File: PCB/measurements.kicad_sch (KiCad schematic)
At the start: 32 parts

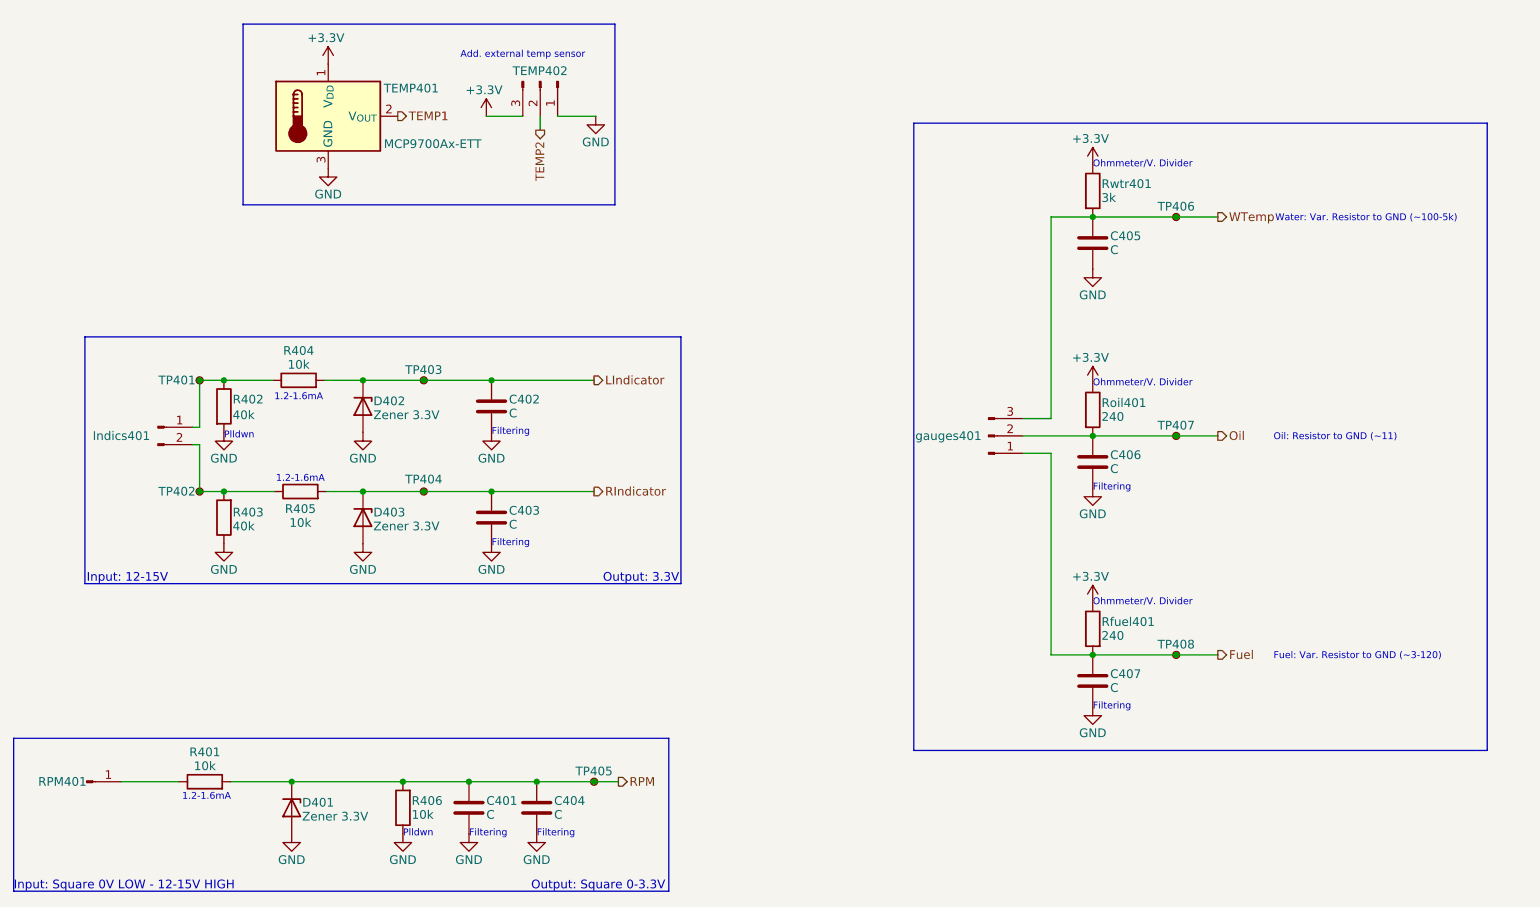
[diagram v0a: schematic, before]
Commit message: Applied recommendations from my coworker; Fixed badly placed filter caps; Added flyback diode to fan circuit; Applied larger grid and some spacing to the schematics; And some other small adjustments
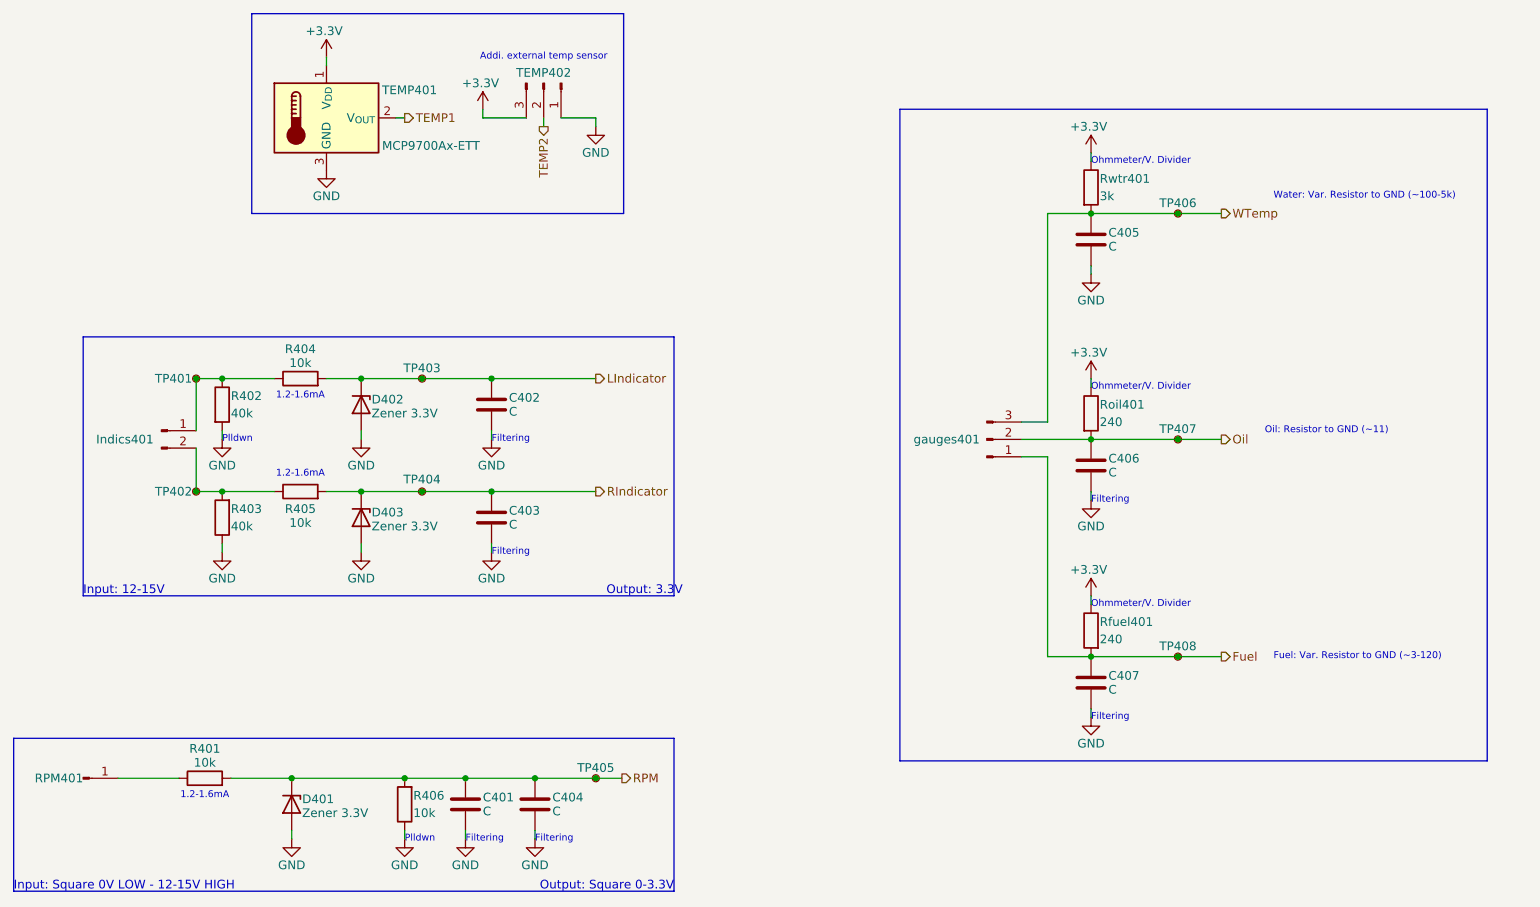
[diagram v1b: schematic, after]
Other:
- note added: "Addi. external temp sensor"
- note removed: "Add. external temp sensor"
- title: (none) -> Measurements
- moved on the sheet: C401, C404, C405, C406, D401, Indics401, R401, R406, RPM401, Roil401, Rwtr401, TEMP402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

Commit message: Changed some resistor and capacitor values;Added additional input electrolytic cap;Selected LCSC parts;Added diode footprint;Removed 3.3V power supply and decreased the output of the 5V supply to 3.3V;Added flyback diode on the fan circuit;Added LDO between the USB-C VBUS and the 5V rail
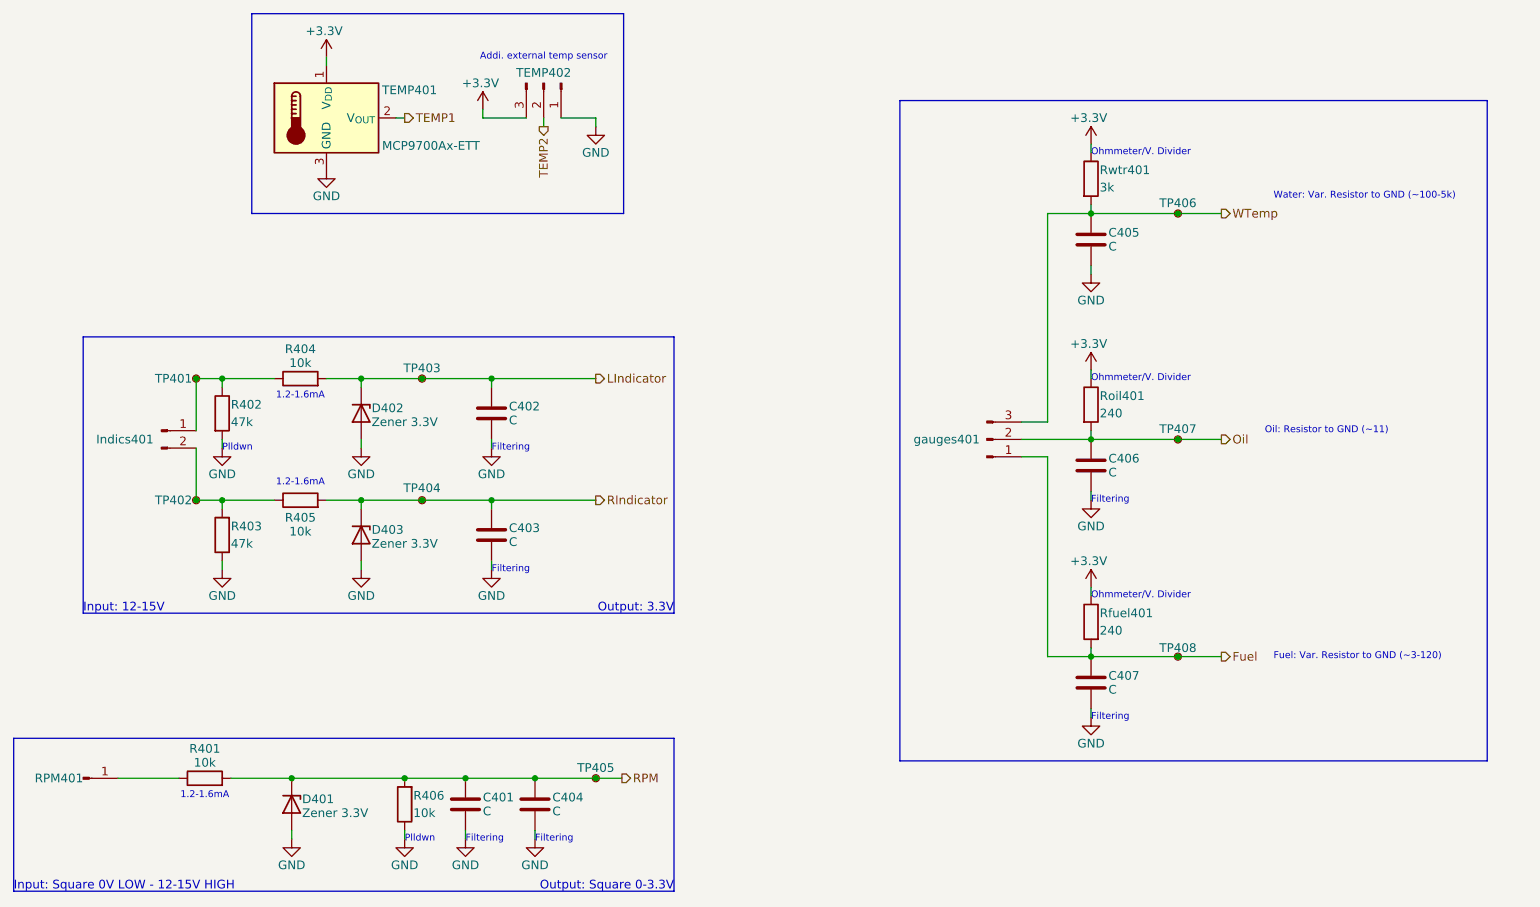
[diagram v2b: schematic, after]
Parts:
- D401, D402, D403: footprint Diode_SMD:D_0805_2012Metric -> Diode_SMD:D_SOD-123
- R401, R404, R405, R406: footprint Resistor_SMD:R_0805_2012Metric -> Resistor_SMD:R_0603_1608Metric
- R402, R403: value 40k -> 47k
- RPM401: now left out of the parts list
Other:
- moved on the sheet: C402, C403, D402, D403, R402, R403, R405, Rfuel401, Roil401, Rwtr401, TP402, TP404
